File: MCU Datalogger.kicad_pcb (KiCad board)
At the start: 2 copper layers, 53.8 x 35.8 mm, 30 parts, among them J1 Conn_01x04_Pin, J2 Conn_01x09_Pin, J3 Conn_01x04_Pin, J4 Conn_02x03_Odd_Even, U1 24LC1025, U2 24LC1025, U3 DS1337S_, U4 ATMEGA328P-AU, Y1 32.768 KHz, Y2 16 MHz

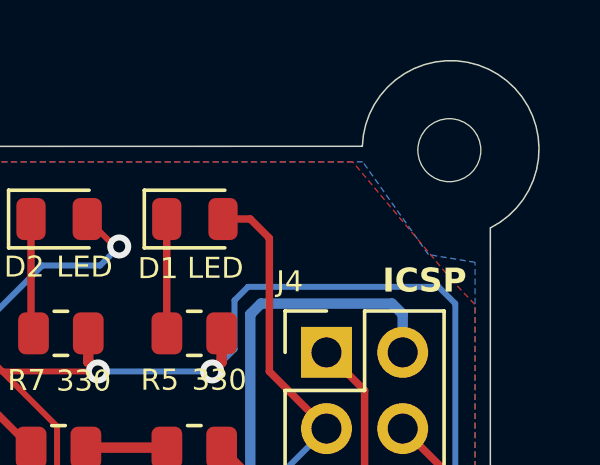
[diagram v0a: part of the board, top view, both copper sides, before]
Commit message: Added gerber directories to .gitignore
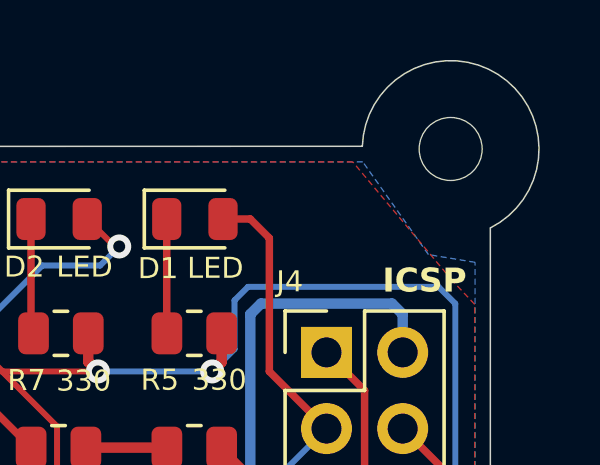
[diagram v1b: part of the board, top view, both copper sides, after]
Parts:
- moved H3 0.06 mm to (114.0, 68.2)
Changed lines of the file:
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@@
 	(footprint "MountingHole:MountingHole_2.1mm"
 		(layer "F.Cu")
-		(at 113.95 68.19)
+		(at 113.994 68.15)
 		(descr "Mounting Hole 2.1mm, no annular, generated by kicad-footprint-generator mountinghole.py")
 		(tags "mountinghole")

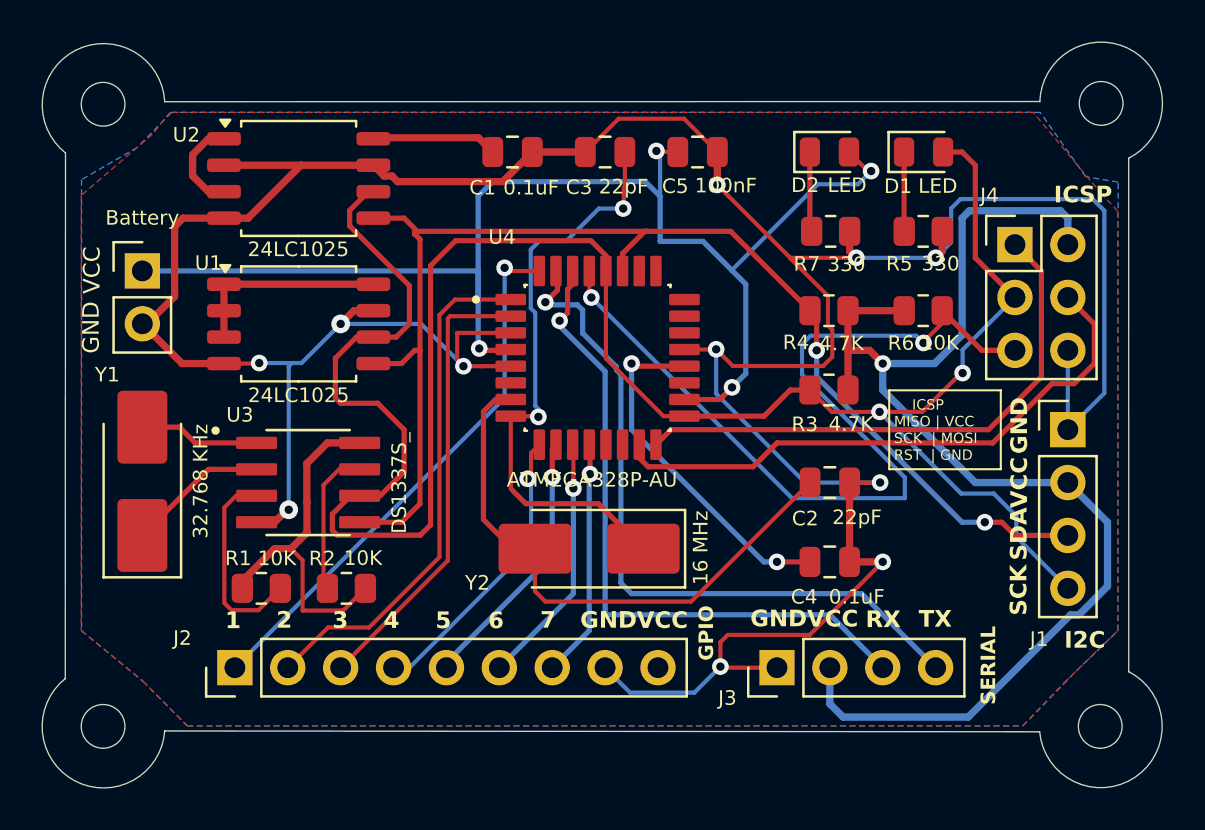
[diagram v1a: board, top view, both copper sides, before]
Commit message: Initial routing 4 layers
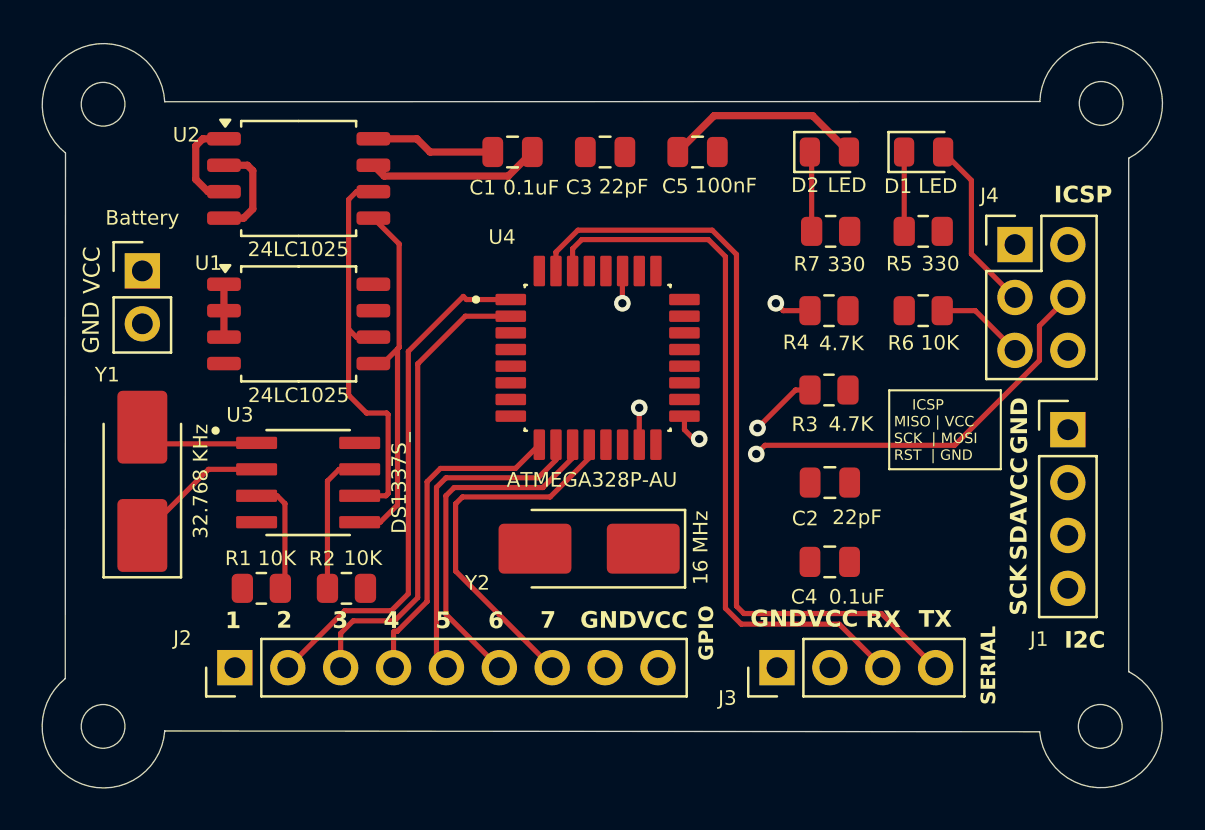
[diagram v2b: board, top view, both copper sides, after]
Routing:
- net GND: track 167.4 -> 13.2 mm, vias 11 -> 0
- net /Vcc: track 164.9 -> 22.9 mm, vias 5 -> 0
- net /SCK: track 103.4 -> 35.9 mm
- net /RESET: track 42.7 -> 4.28 mm, vias 2 -> 0
- net /SDA: track 62.9 -> 28.8 mm
- net Net-(U4-PB7): track 28.6 -> 0.00 mm, vias 2 -> 0
- net Net-(U4-PB6): track 27.6 -> 0.00 mm
- net /MISO: track 26.7 -> 0.00 mm
- net /D2: track 26.3 -> 0.00 mm, vias 1 -> 0
- net Net-(U4-AREF): track 17.0 -> 0.00 mm, vias 2 -> 0
- net /D8: track 11.5 -> 17.8 mm, vias 1 -> 0
- net /D7: track 12.2 -> 16.8 mm, vias 1 -> 0
- net Net-(U3-~{INTA}): track 9.64 -> 5.68 mm
- net /TX: track 34.4 -> 38.2 mm, vias 1 -> 0
- net /D6: track 12.6 -> 15.9 mm, vias 1 -> 0
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- removed copper zone on F.Cu, net /Vcc
- removed copper zone on B.Cu, net GND
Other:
- copper layers 2 -> 4

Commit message: Completed routing 4 layers
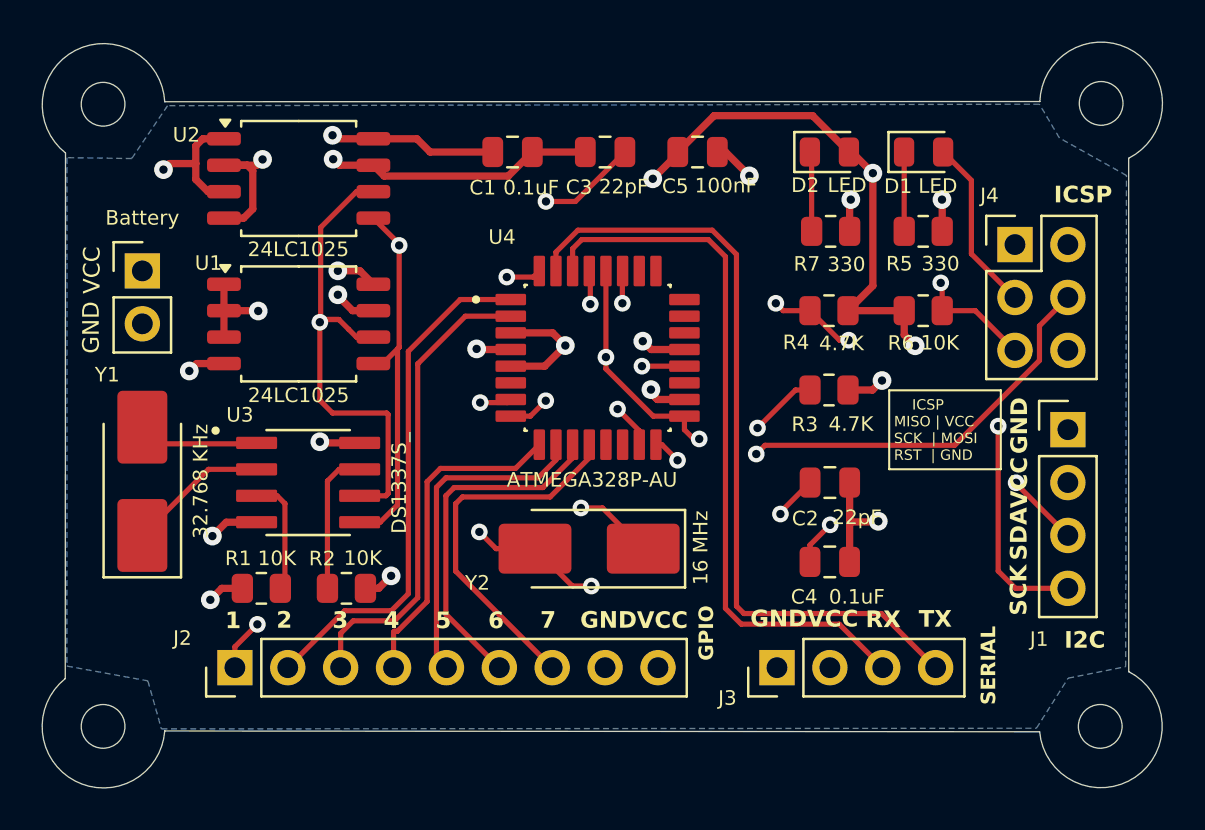
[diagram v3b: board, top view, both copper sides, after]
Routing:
- net /SCK: track 35.9 -> 97.1 mm, vias 2 -> 5
- net /Vcc: track 22.9 -> 55.9 mm, vias 0 -> 13
- net GND: track 13.2 -> 44.4 mm, vias 0 -> 11
- net /D2: track 0.00 -> 30.2 mm, vias 0 -> 2
- net /SDA: track 28.8 -> 57.7 mm, vias 2 -> 5
- net Net-(U4-PB6): track 0.00 -> 26.8 mm, vias 0 -> 4
- net Net-(U4-PB7): track 0.00 -> 26.0 mm, vias 0 -> 3
- net /MISO: track 0.00 -> 21.8 mm, vias 0 -> 1
- net /RESET: track 4.28 -> 24.5 mm, vias 0 -> 2
- net Net-(U4-AREF): track 0.00 -> 17.7 mm, vias 0 -> 2
- net /MOSI: track 27.4 -> 29.0 mm
- added copper zone on In2.Cu, net /Vcc
- added copper zone on B.Cu, net GND
